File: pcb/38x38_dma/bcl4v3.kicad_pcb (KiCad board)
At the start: 2 copper layers, 38.1 x 37.8 mm, 24 parts, among them J1 Conn_01x04, J10 Conn_01x04, J2 Conn_01x04, J3 Conn_01x04, J4 Conn_01x04, J5 Conn_01x04, J6 Conn_01x04, J7 Conn_01x04, J8 Conn_01x04, J9 USB_MICRO-B_FEMALE-SMT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

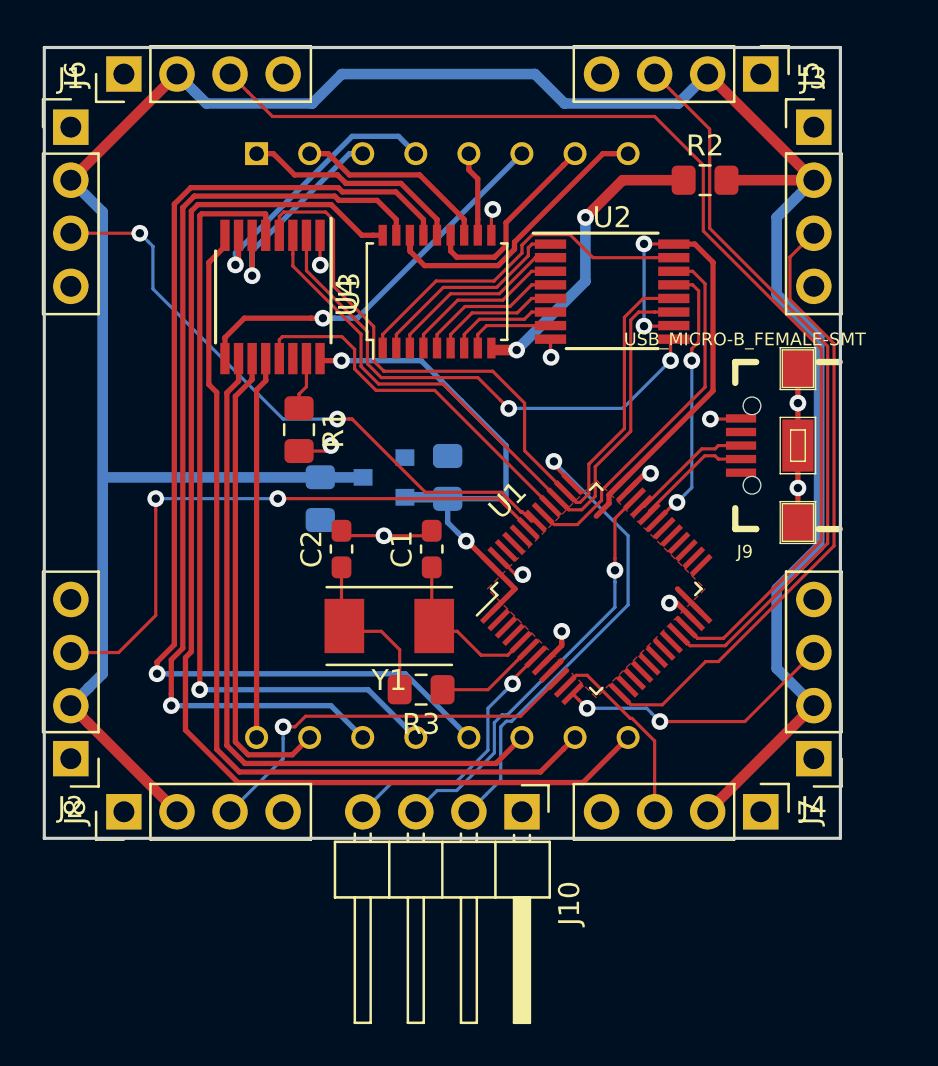
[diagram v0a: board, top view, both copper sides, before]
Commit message: Board update
fully routed PCB
indicator LED added
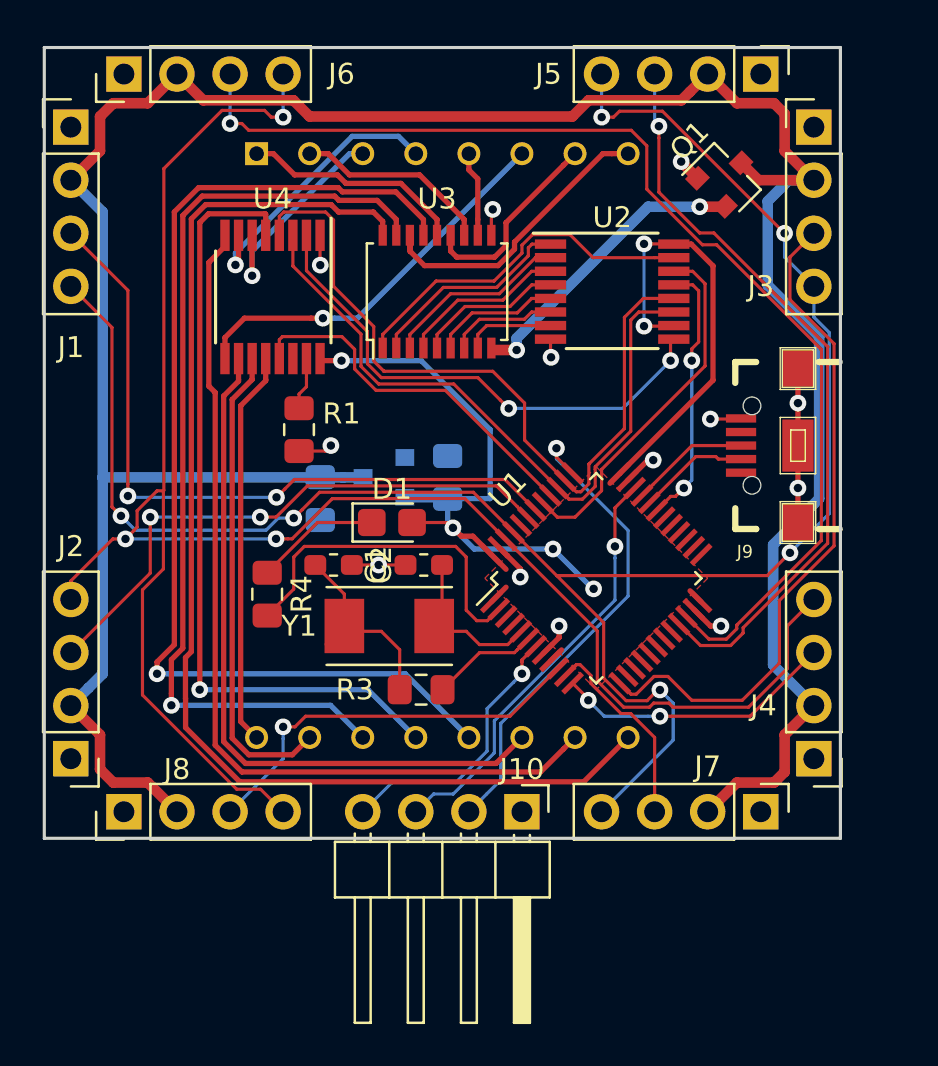
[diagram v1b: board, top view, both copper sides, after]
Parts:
- removed R2: 0R, Resistor_SMD:R_0805_2012Metric_Pad1.15x1.40mm_HandSolder
- added D1: LED, LED_SMD:LED_0805_2012Metric_Castellated, F.Cu at (130.6, 86.9)
- added Q1: IRLML6402, Package_TO_SOT_SMD:SOT-23, F.Cu at (146.6, 70.4)
- added R4: R, Resistor_SMD:R_0805_2012Metric_Pad1.15x1.40mm_HandSolder, F.Cu at (124.7, 90.3)
- moved C1 0.85 mm to (132.2, 88.9), turned to 180 degrees
- moved C2 0.85 mm to (127.8, 88.9), turned to 0 degrees
- moved U1 0.51 mm to (140.4, 89.6)
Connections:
- U1 pad 2: Net-(U1-Pad2) -> /LED
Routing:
- net /I2C_SDA: track 0.00 -> 94.3 mm, vias 0 -> 6
- net /I2C_SCL: track 0.00 -> 94.0 mm, vias 0 -> 3
- net /LED: track 0.00 -> 16.5 mm
- net Net-(D1-Pad1): track 0.00 -> 6.00 mm
- net /UART1_TX: track 29.1 -> 34.2 mm
- net +3V3: track 51.4 -> 56.1 mm, vias 4 -> 6
- net VCC: track 127.6 -> 132.1 mm
- net /UART2_RX: track 29.9 -> 32.4 mm
- net Net-(C2-Pad1): track 7.51 -> 9.66 mm
- net /UART1_RX: track 28.8 -> 27.4 mm
- net /UART3_RX: track 53.4 -> 54.5 mm, vias 0 -> 1
- net /CAT_STROBE: track 37.7 -> 36.7 mm
- net /UART3_TX: track 35.3 -> 36.0 mm, vias 0 -> 1
- net /CAT_CLK: track 33.3 -> 32.6 mm
- net /COL_8: track 18.3 -> 18.9 mm
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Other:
- rule solder_mask_min_width: 0.25 -> 0.1524

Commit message: PCB and schematics updates
- exchange STM32F070 with STM32F072 (USB w/o HSE)
- remove xtal and related components
- add boot mode jumper pads (NO)
- connect USB_VBUS with VCC via jumper (NC)
- smaller clearance for pad to solder mask
- add local library directory for externally imported
  symbols, footprints and 3D models

PCB outline
add small cut-out for USB receptacle
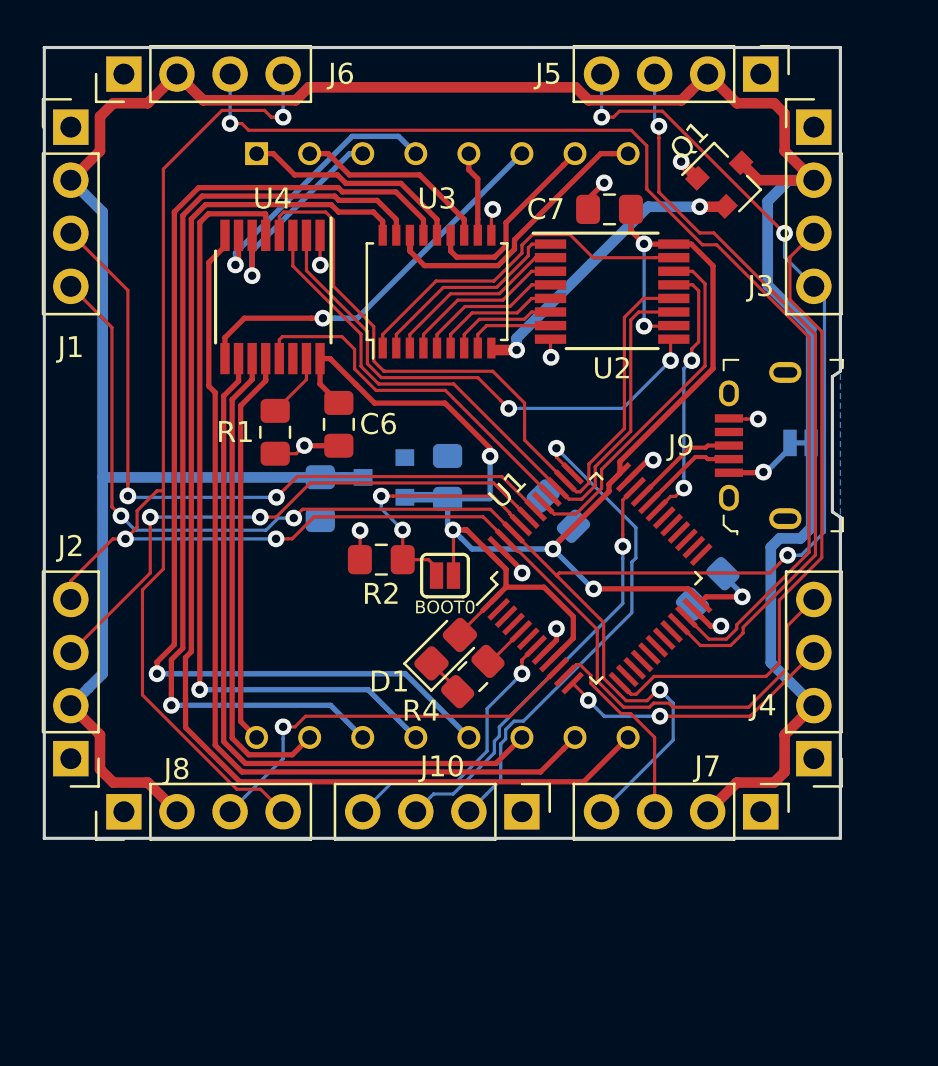
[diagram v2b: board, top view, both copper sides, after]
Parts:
- removed C1, C2: 20pF, Capacitor_SMD:C_0603_1608Metric_Pad1.05x0.95mm_HandSolder
- removed R3: 220R, Resistor_SMD:R_0805_2012Metric_Pad1.15x1.40mm_HandSolder
- removed Y1: 8Mhz, Crystal:Crystal_SMD_Abracon_ABM7-2Pin_6.0x3.5mm
- added BOOT0: Jumper_2_Open, Jumpers:SMT-JUMPER_2_NO_SILK, F.Cu at (133.2, 89.4)
- added C5: C_Small, Capacitor_SMD:C_0805_2012Metric_Pad1.15x1.40mm_HandSolder, B.Cu at (138.6, 86.3)
- added C6: C_Small, Capacitor_SMD:C_0805_2012Metric_Pad1.15x1.40mm_HandSolder, F.Cu at (128.1, 82.2)
- added C7: C_Small, Capacitor_SMD:C_0805_2012Metric_Pad1.15x1.40mm_HandSolder, F.Cu at (141.1, 71.9)
- added C8: C_Small, Capacitor_SMD:C_0805_2012Metric_Pad1.15x1.40mm_HandSolder, B.Cu at (145.8, 90.1)
- added JP1: Jumper, Jumpers:SMT-JUMPER_2_NC_TRACE_NO-SILK, B.Cu at (150.2, 83.1)
- added R2: 1k, Resistor_SMD:R_0805_2012Metric_Pad1.15x1.40mm_HandSolder, F.Cu at (130.1, 88.7)
- C3, C4: value C_Small -> 4.7u
- DS1: value TC15-11SRWA -> LDM-1588BS
- J10: footprint Connector_PinHeader_2.54mm:PinHeader_1x04_P2.54mm_Horizontal -> Connector_PinHeader_2.54mm:PinHeader_1x04_P2.54mm_Vertical
- J9: value USB_MICRO-B_FEMALE-SMT -> 10118194-0001LF; footprint Connectors:USB-B-MICRO-SMD -> digikey-footprints:USB_Micro_B_Female_10118194-0001LF
- R1: value R -> 1k
- R4: value R -> 680R
- U1: value STM32F070CBTx -> STM32F072CBTx
- moved R4 10.6 mm to (134.5, 94.3), turned to 45 degrees
- moved D1 6.59 mm to (133.2, 93.0), turned to 45 degrees
- moved J9 3.30 mm to (146.8, 83.2), turned to 90 degrees
- moved R1 1.15 mm to (125.0, 82.6)
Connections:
- U1 pad 2: /LED -> Net-(U1-Pad2)
- U1 pad 44: Net-(U1-Pad44) -> /BOOT0
- U1 pad 5: /OSC_IN -> /LED
- U1 pad 6: /OSC_OUT -> Net-(U1-Pad6)
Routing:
- net +3V3: track 56.1 -> 82.4 mm, vias 6 -> 7
- net /LED: track 16.5 -> 2.17 mm
- net /BOOT0: track 0.00 -> 12.5 mm, vias 0 -> 2
- net Net-(C2-Pad1): track 9.66 -> 0.00 mm
- net /OSC_IN: track 7.75 -> 0.00 mm
- net GND: track 24.5 -> 18.2 mm, vias 13 -> 12
- net /OSC_OUT: track 5.11 -> 0.00 mm
- net Net-(D1-Pad1): track 6.00 -> 1.87 mm
- net /USB_VBUS: track 0.00 -> 3.60 mm, vias 0 -> 1
- net /UART2_RX: track 32.4 -> 31.0 mm
- net /I2C_SCL: track 94.0 -> 93.3 mm
- net /USB_D-: track 5.35 -> 6.01 mm
- net Net-(R1-Pad1): track 2.52 -> 3.12 mm
- net /USB_D+: track 5.73 -> 5.15 mm
- net /SWCLK: track 23.5 -> 24.1 mm
- removed copper zone on F.Cu, net +3V3
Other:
- outline, holes or cut-outs redrawn
- rule pad_to_mask_clearance: 0.051 -> 0.0508
- rule solder_mask_min_width: 0.1524 -> 0.0508

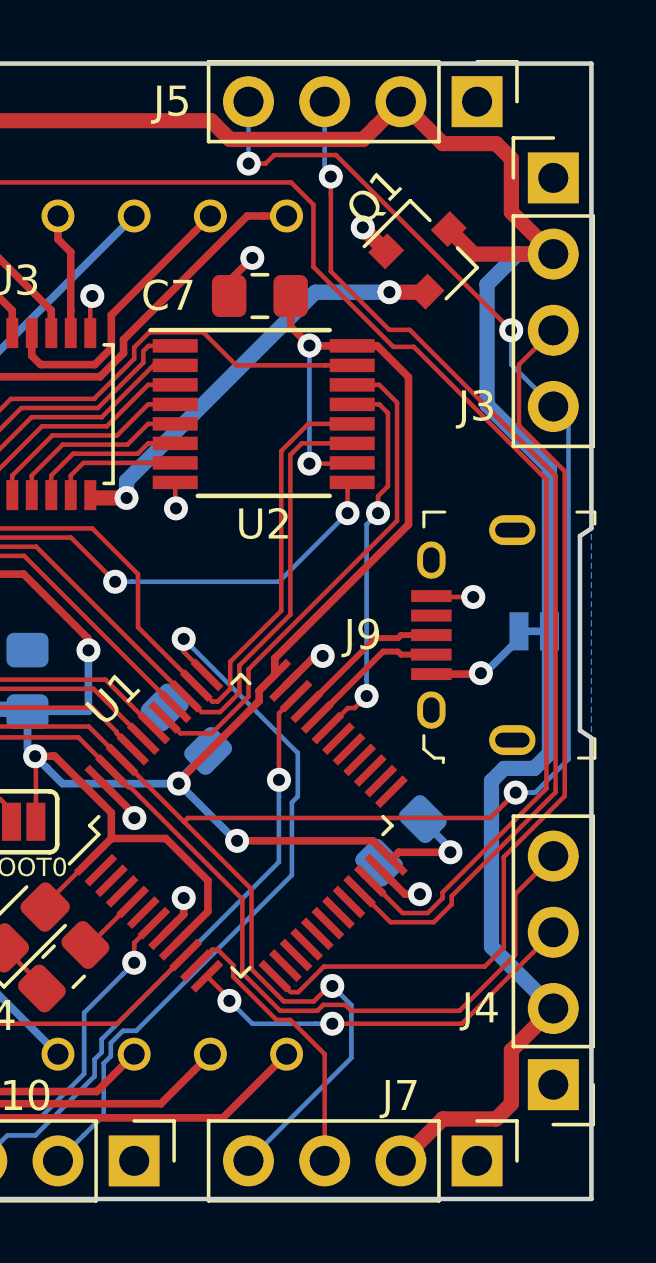
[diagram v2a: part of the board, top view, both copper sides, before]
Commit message: PCB updates for panelization
- place USB receptacle and edge cut-out smack center of the right board edge
- rounded cut-out (.4mm radius) to allow routing it out using a single
  0.8mm wide slot.
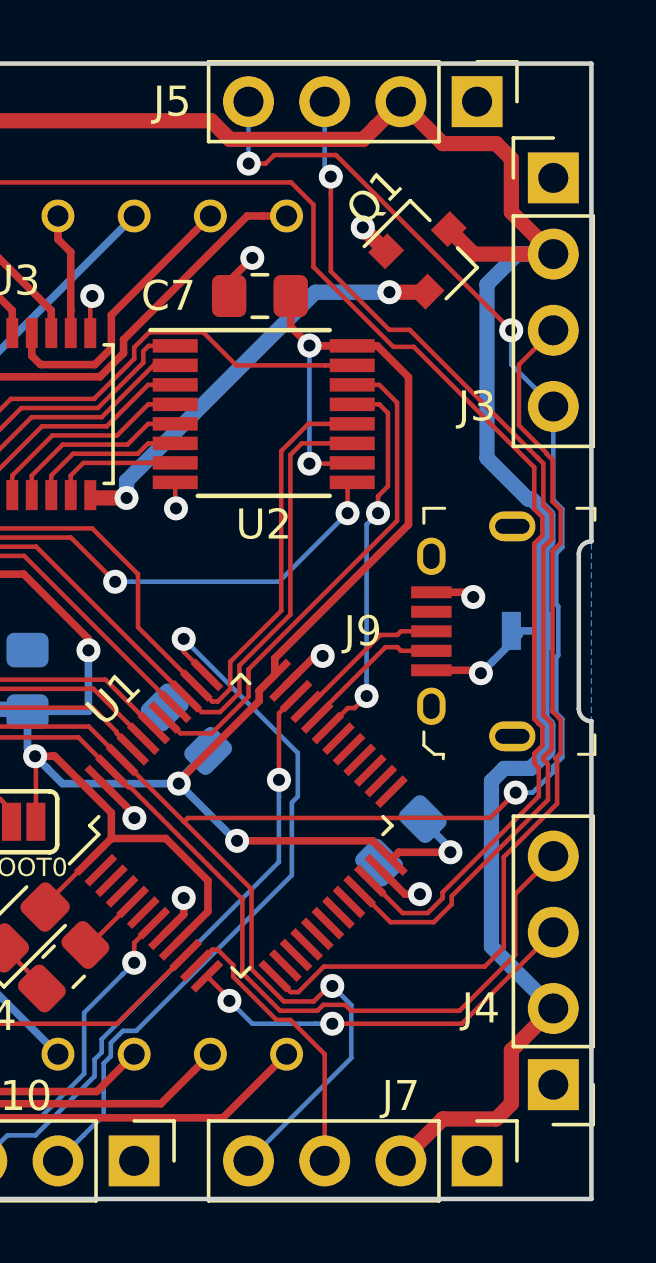
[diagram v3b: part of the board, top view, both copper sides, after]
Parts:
- moved JP1 0.25 mm to (149.9, 83.1)
- moved J9 0.13 mm to (146.8, 83.1)
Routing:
- net GND: track 18.2 -> 18.8 mm
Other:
- outline, holes or cut-outs redrawn

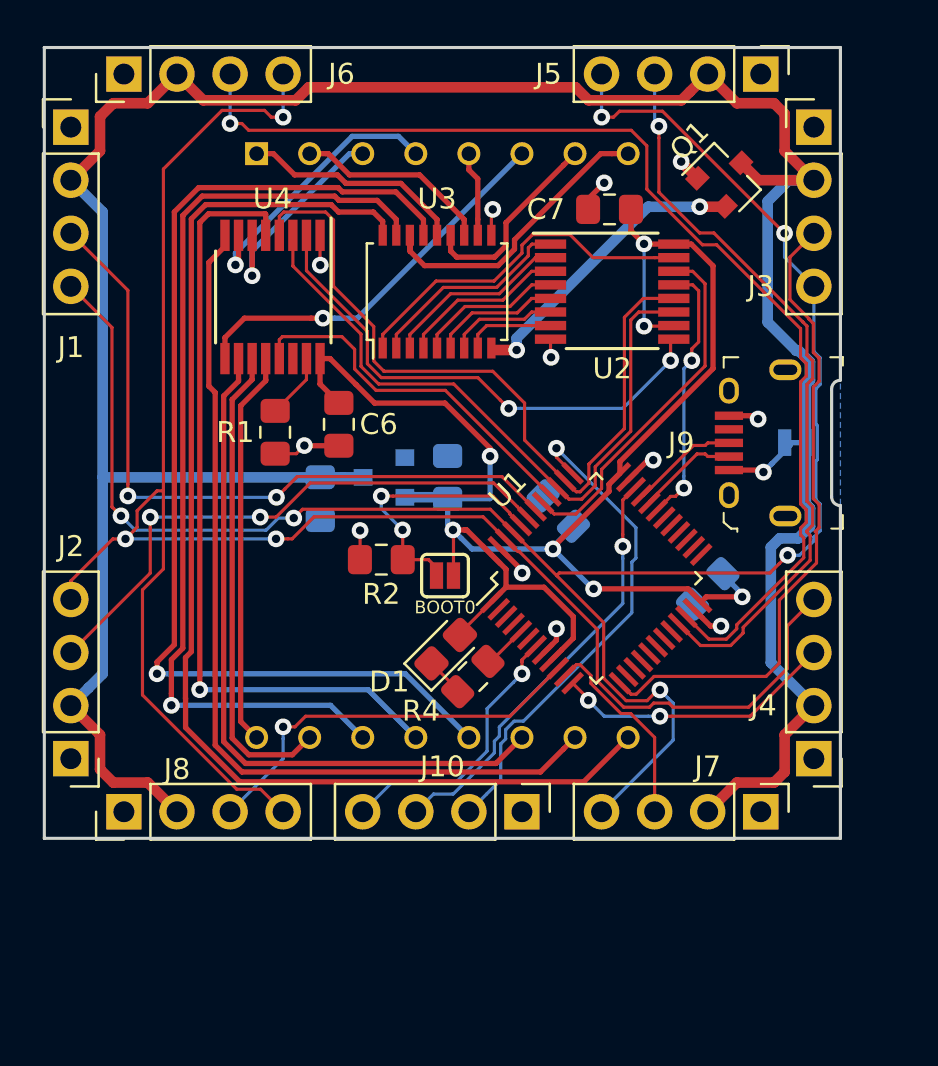
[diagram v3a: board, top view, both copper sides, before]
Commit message: PCB and schematics cleanup
resize PCB to exactly 38x38mm, center the LED matrix
add OSHW logo to silk screen, add copyright information
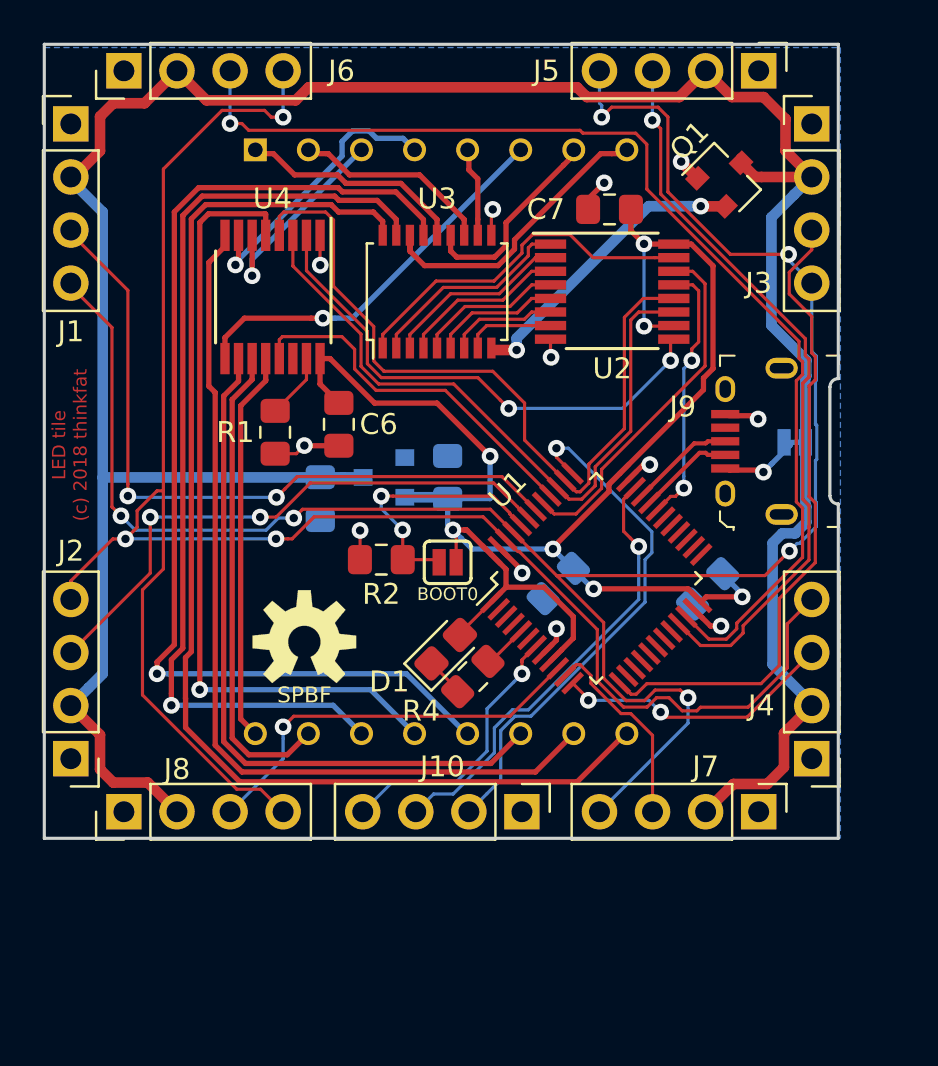
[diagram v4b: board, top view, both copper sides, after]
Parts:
- added ?: , Aesthetics:OSHW-LOGO-M, F.Cu at (126.4, 92.6)
- moved C5 3.47 mm to (138.6, 89.8), turned to 225 degrees
- moved BOOT0 0.65 mm to (133.3, 88.8)
- moved J9 0.19 mm to (146.6, 83.0)
- moved DS1 0.19 mm to (124.1, 69.0)
- moved J3 0.18 mm to (150.7, 67.8)
- moved J5 0.18 mm to (148.2, 65.3)
- moved J6 0.15 mm to (117.8, 65.3)
- moved J1 0.15 mm to (115.3, 67.8)
- moved J4 0.10 mm to (150.7, 98.2)
- moved J7 0.10 mm to (148.2, 100.7)
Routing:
- net /I2C_SDA: track 93.9 -> 96.3 mm
- net +3V3: track 82.4 -> 80.6 mm
- net VCC: track 132.4 -> 130.9 mm
- net /USB_D-: track 6.12 -> 4.84 mm
- net /SWCLK: track 24.1 -> 25.2 mm
- net /SWDIO: track 20.4 -> 21.4 mm
- net /UART3_RX: track 54.2 -> 53.6 mm
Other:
- board size 38.1 x 37.8 mm -> 38 x 38 mm
- board text added: "LED tile (c) 2018 thinkfat"
- board text added: "SPBF"

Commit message: Fix reverse voltage protection, cleanups
- power from USB doesn't need to go through protection FET
- power to 3.3V LDO _must_ got through protection FET
- add OSHW logo also to schematics so that it doesn't vanish if you
  sync PCB and schematics
- modify copyright info a bit
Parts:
- removed ?: , Aesthetics:OSHW-LOGO-M
- added LOGO1: OSHW-LOGOM, OSHW-LOGO-M, F.Cu at (122.3, 89.9)
- C5, C6, C7, C8: value C_Small -> 100n
- moved C3 5.12 mm to (129.2, 81.0), turned to 90 degrees
- moved BOOT0 4.46 mm to (129.3, 90.8)
- moved JP1 3.07 mm to (146.8, 82.8), turned to 90 degrees
- moved D1 0.12 mm to (133.1, 92.9)
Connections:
- C3 pad 1: VCC -> +5V
- JP1 pad 2: VCC -> +5V
- U5 pad 3: VCC -> +5V
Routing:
- net +5V: track 14.2 -> 38.1 mm
- net VCC: track 130.9 -> 119.0 mm
- net +3V3: track 80.6 -> 85.1 mm
- net /BOOT0: track 12.5 -> 14.3 mm
